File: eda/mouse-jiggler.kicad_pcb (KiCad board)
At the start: 2 copper layers, 71.1 x 54.6 mm, 16 parts, among them J1 Screw_Terminal_01x02, J2 Screw_Terminal_01x02, Q1 IRFZ44NPBF, SW1 SW_DPDT_x2, U1 NE555P

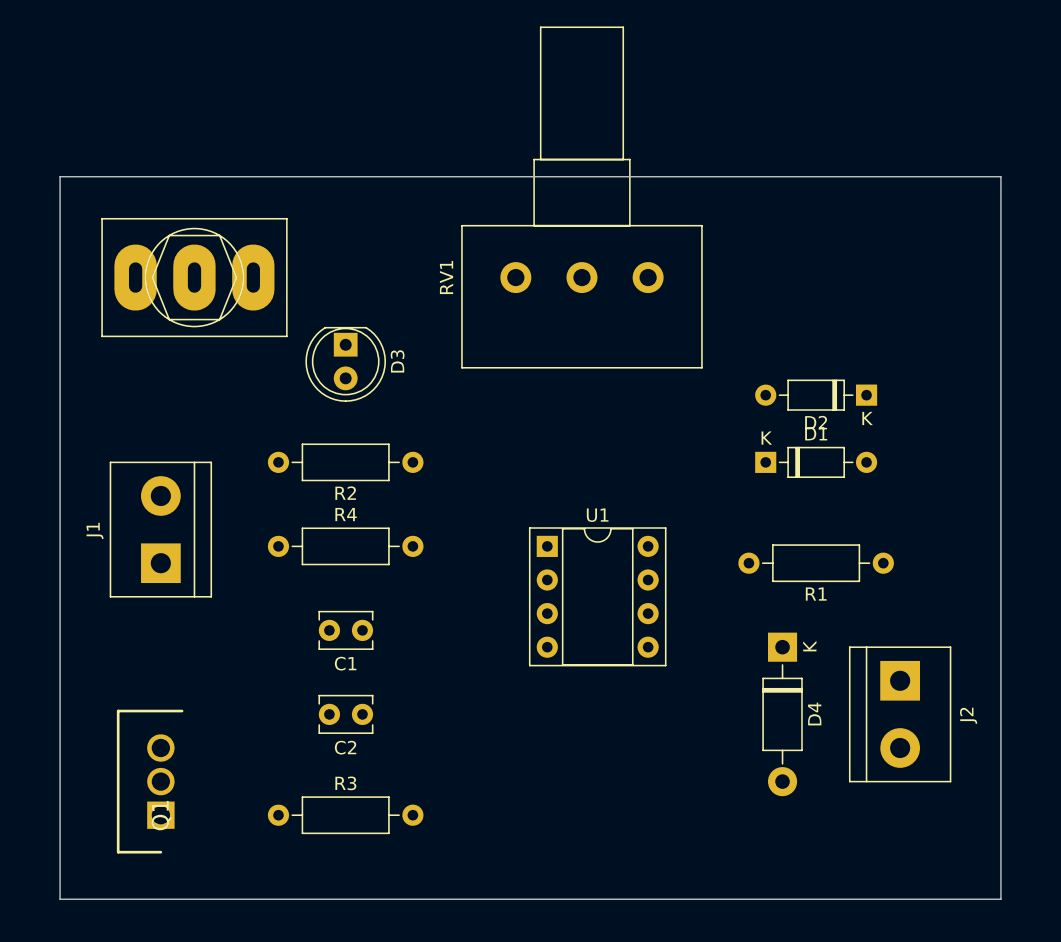
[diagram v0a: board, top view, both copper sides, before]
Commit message: fix toggle switch footprint and generate gerber
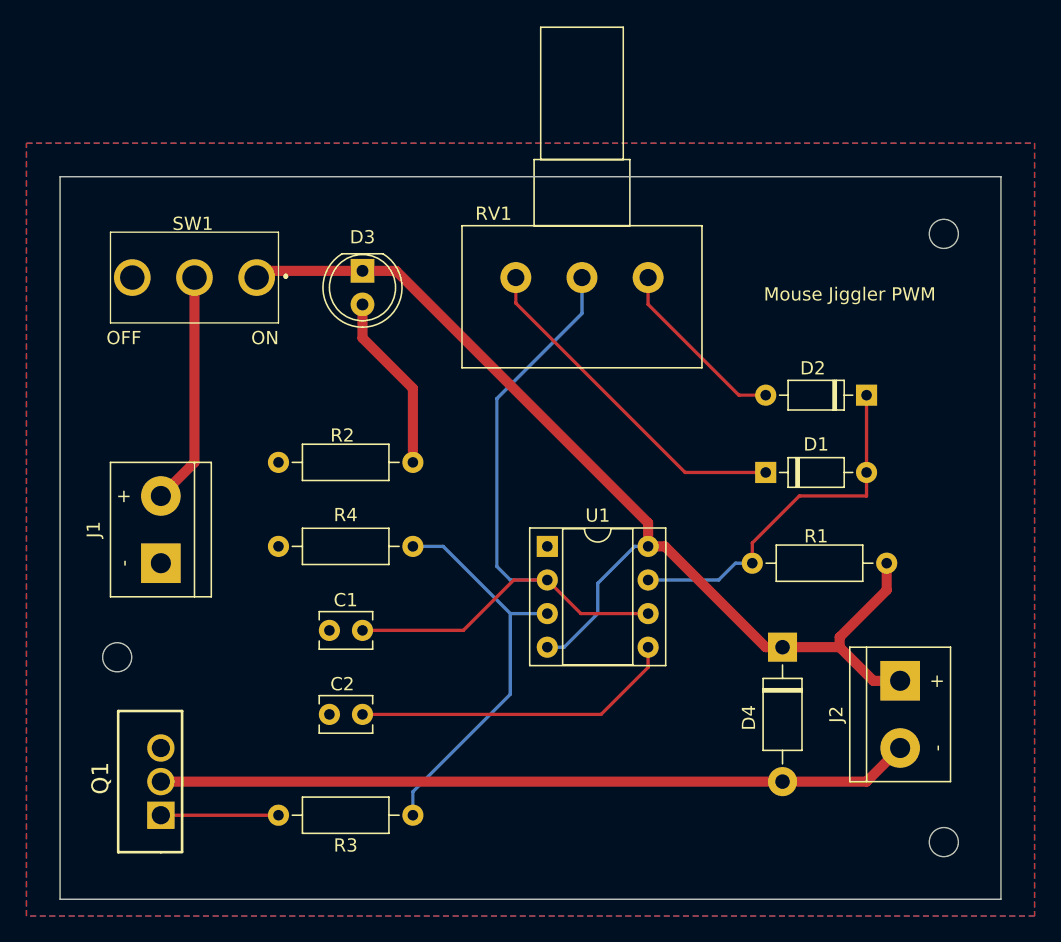
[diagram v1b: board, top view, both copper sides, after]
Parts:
- added REF**: MountingHole_2.2mm_M2, MountingHole:MountingHole_2.2mm_M2, F.Cu at (178.6, 75.4)
- added REF**: MountingHole_2.2mm_M2, MountingHole:MountingHole_2.2mm_M2, F.Cu at (116.1, 107.4)
- added REF**: MountingHole_2.2mm_M2, MountingHole:MountingHole_2.2mm_M2, F.Cu at (178.6, 121.4)
- SW1: footprint toggle switch:SW_Toggle_Blue_wSlots -> 100SP1T1B4M2QE-switch:100SP1T1B4M2QE
- moved D3 5.73 mm to (134.6, 78.2)
- moved D1 0.76 mm to (165.1, 93.5)
- moved R1 0.25 mm to (174.2, 100.3)
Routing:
- net Net-(D3-Pad1): track 0.00 -> 82.9 mm
- net Net-(D4-Pad2): track 0.00 -> 56.9 mm
- net Net-(C1-Pad1): track 0.00 -> 53.0 mm
- net Net-(R3-Pad2): track 0.00 -> 30.6 mm
- net Net-(D1-Pad2): track 0.00 -> 27.7 mm
- net Net-(D1-Pad1): track 0.00 -> 26.1 mm
- net Net-(C2-Pad1): track 0.00 -> 24.6 mm
- net Net-(J1-Pad2): track 0.00 -> 17.6 mm
- net Net-(D2-Pad2): track 0.00 -> 13.8 mm
- net Net-(D3-Pad2): track 0.00 -> 13.5 mm
- net Net-(Q1-Pad1): track 0.00 -> 8.89 mm
- added copper zone on B.Cu, net GND
- added copper zone on F.Cu, net GND
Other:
- rule pad_to_mask_clearance: 0.05 -> 0
- board text added: "+"
- board text added: "-"
- board text added: "Mouse Jiggler PWM"
- board text added: "OFF"
- board text added: "ON"
